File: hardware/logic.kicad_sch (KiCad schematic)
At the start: 23 parts, among them IC1 UCC2946DG4, IC2 SN74LVC1G74DCTR, IC3 SN74LVC1G74DCTR, Q1 BSS123, U1 74157, U2 4011, U3 4081, U4 4071

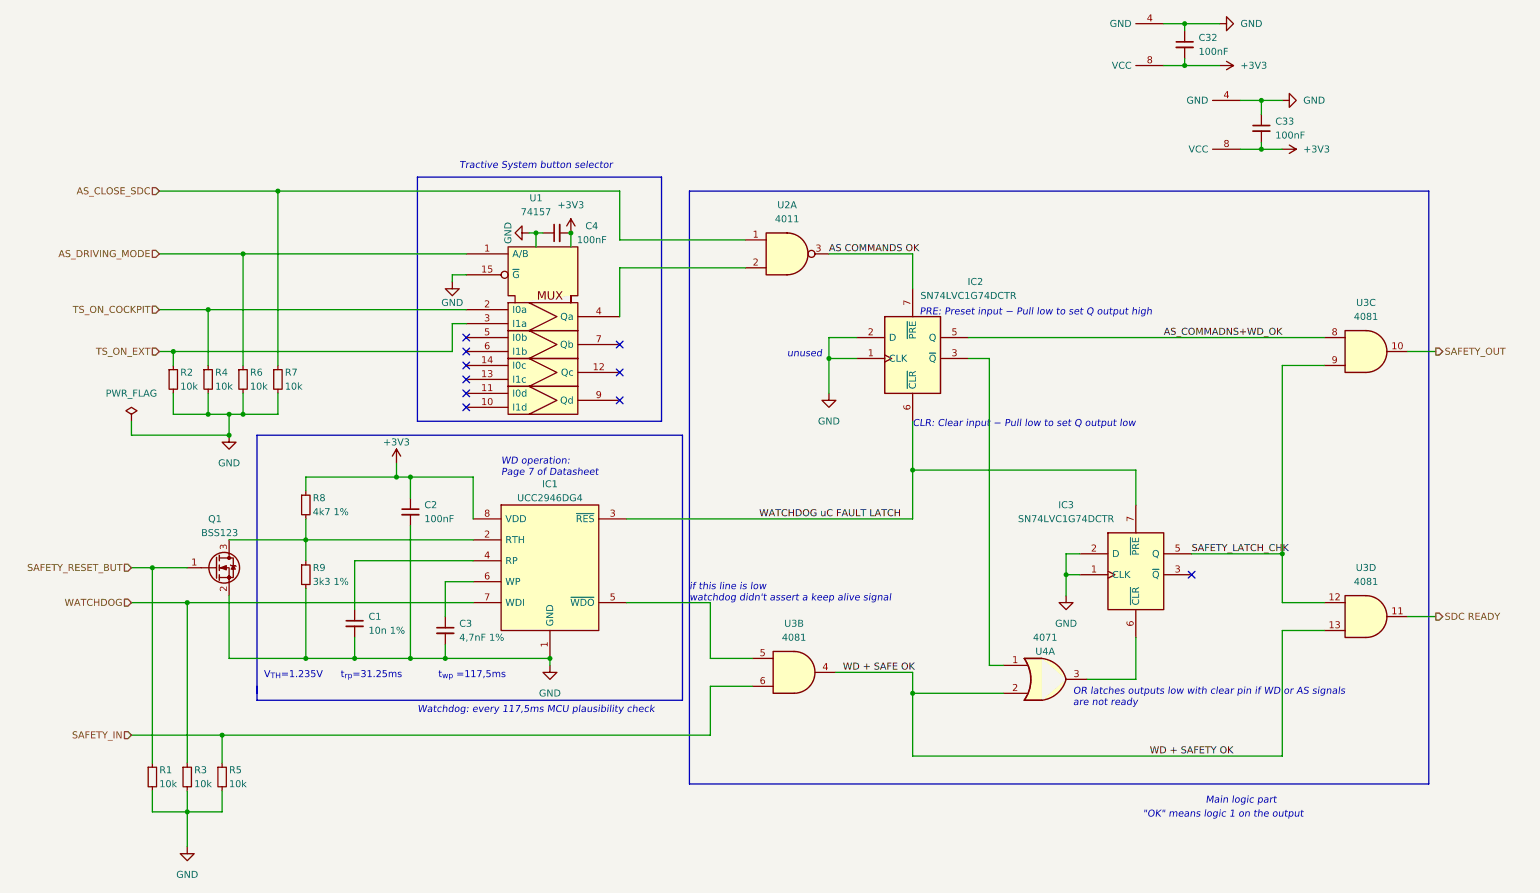
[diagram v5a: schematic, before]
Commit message: 0xERC State
Schematic needs only simulation and veryfying component choice for now
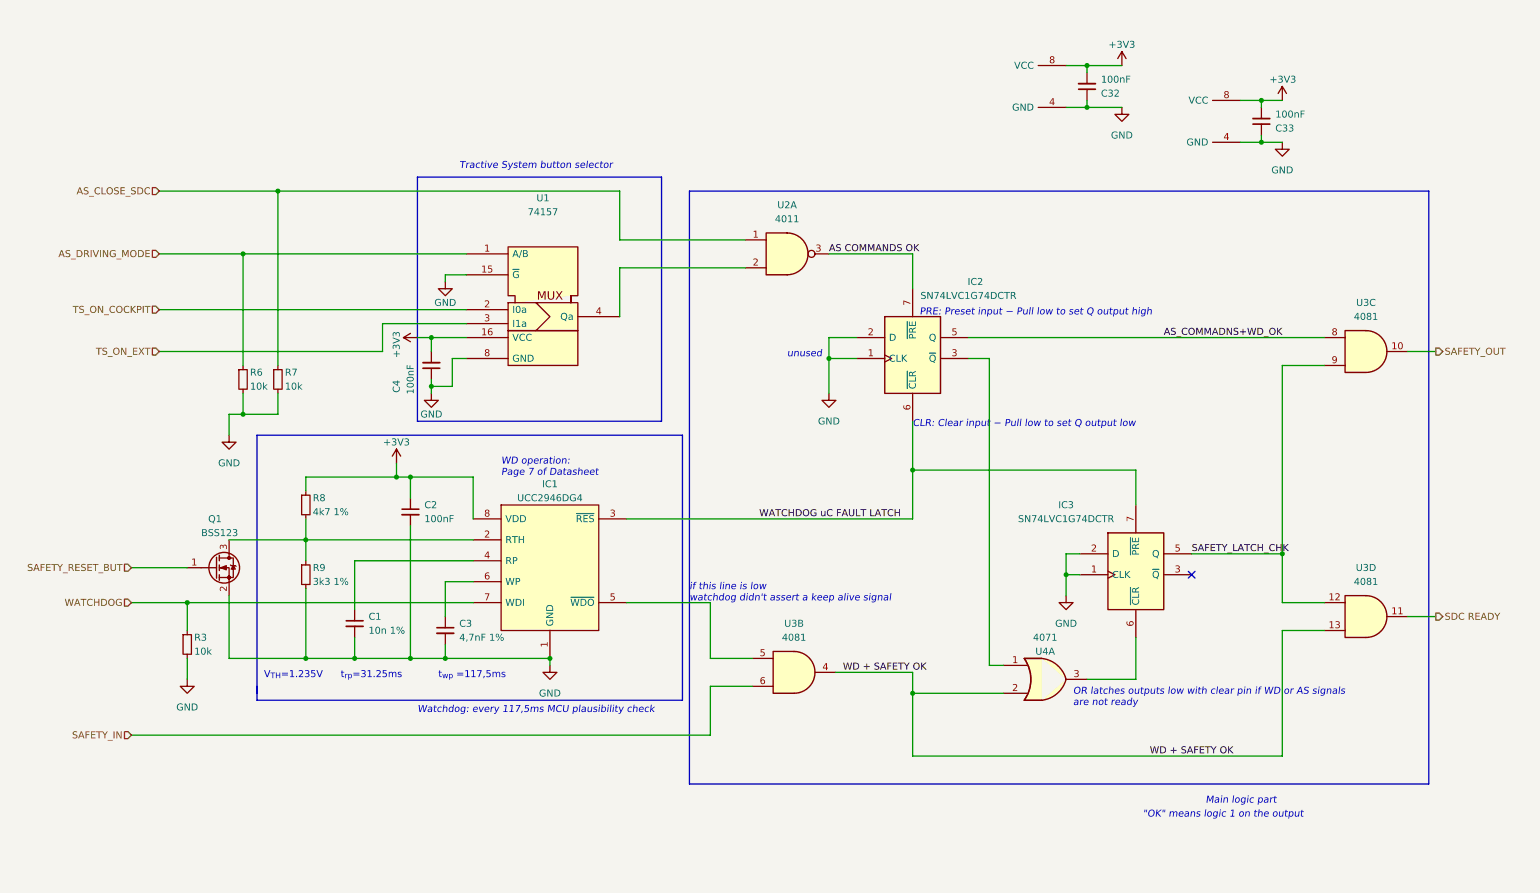
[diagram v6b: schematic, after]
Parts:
- removed R1, R2, R4, R5: 10k, Resistor_SMD:R_0603_1608Metric, symbol Device:R_Small
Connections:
- net WD + SAFE OK renamed WD + SAFETY OK
- no-connect marks 10 -> 1
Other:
- moved on the sheet: C32, C33, C4, IC2, R3

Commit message: working simulations, assigned footprints
"nightly" relase
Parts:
- U1: footprint Resistor_SMD:R_0603_1608Metric -> Package_SO:VSSOP-8_2.3x2mm_P0.5mm
- U2, U3, U4: footprint (none) -> Package_SO:TSSOP-14_4.4x5mm_P0.65mm
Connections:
- net WATCHDOG uC FAULT LATCH renamed RESET BUTTON LATCH
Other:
- note added: "pull RTH low to reset"
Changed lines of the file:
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@@
+    (stroke (width 0) (type default) (color 0 0 0 0))
+  )
+  (wire (pts (xy 187.96 81.28) (xy 187.96 100.33))
     (stroke (width 0) (type default) (color 0 0 0 0))
   )
@@
     (stroke (width 0) (type default) (color 0 0 0 0))
   )
+  (wire (pts (xy 187.96 104.14) (xy 187.96 137.16))
+    (stroke (width 0) (type default) (color 0 0 0 0))
+  )
   (wire (pts (xy 83.82 77.47) (xy 86.36 77.47))
     (stroke (width 0) (type default) (color 0 0 0 0))
@@
     (stroke (width 0) (type default) (color 0 0 0 0))
   )
+  (wire (pts (xy 187.96 100.33) (xy 189.23 100.33))
+    (stroke (width 0) (type default) (color 0 0 0 0))
+  )
   (wire (pts (xy 241.3 130.81) (xy 248.92 130.81))
     (stroke (width 0) (type default) (color 0 0 0 0))
@@
     (stroke (width 0) (type default) (color 0 0 0 0))
   )
-  (wire (pts (xy 187.96 81.28) (xy 187.96 137.16))
-    (stroke (width 0) (type default) (color 0 0 0 0))
-  )
   (wire (pts (xy 41.91 135.89) (xy 41.91 139.7))
     (stroke (width 0) (type default) (color 0 0 0 0))
@@
     (stroke (width 0) (type default) (color 0 0 0 0))
   )
+  (wire (pts (xy 189.23 100.33) (xy 189.23 104.14))
+    (stroke (width 0) (type default) (color 0 0 0 0))
+  )
   (wire (pts (xy 158.75 62.23) (xy 173.99 62.23))
     (stroke (width 0) (type default) (color 0 0 0 0))
@@
   )
   (wire (pts (xy 241.3 125.73) (xy 248.92 125.73))
+    (stroke (width 0) (type default) (color 0 0 0 0))
+  )
+  (wire (pts (xy 189.23 104.14) (xy 187.96 104.14))
     (stroke (width 0) (type default) (color 0 0 0 0))
   )
@@
     (effects (font (size 1.27 1.27) italic) (justify left bottom))
   )
+  (text "pull RTH low to reset\n" (at 22.86 116.84 0)
+    (effects (font (size 1.27 1.27)) (justify left bottom))
+  )
   (text "PRE: Preset input − Pull low to set Q output high" (at 175.26 73.66 0)
     (effects (font (size 1.27 1.27) italic) (justify left bottom))
@@
     (effects (font (size 1.27 1.27)) (justify left bottom))
   )
-  (label "WATCHDOG uC FAULT LATCH" (at 146.05 110.49 0)
+  (label "RESET BUTTON LATCH" (at 146.05 110.49 0)
     (effects (font (size 1.27 1.27)) (justify left bottom))
   )
@@
     (property "Reference" "U4" (id 0) (at 198.12 134.62 0))
     (property "Value" "4071" (id 1) (at 198.12 132.08 0))
-    (property "Footprint" "" (id 2) (at 198.12 139.7 0)
+    (property "Footprint" "Package_SO:TSSOP-14_4.4x5mm_P0.65mm" (id 2) (at 198.12 139.7 0)
       (effects (font (size 1.27 1.27)) hide)
     )
@@
     (property "Reference" "U3" (id 0) (at 256.54 119.38 0))
     (property "Value" "4081" (id 1) (at 256.54 121.92 0))
-    (property "Footprint" "" (id 2) (at 256.54 128.27 0)
+    (property "Footprint" "Package_SO:TSSOP-14_4.4x5mm_P0.65mm" (id 2) (at 256.54 128.27 0)
       (effects (font (size 1.27 1.27)) hide)
     )
@@
     (property "Reference" "U3" (id 0) (at 256.54 71.12 0))
     (property "Value" "4081" (id 1) (at 256.54 73.66 0))
-    (property "Footprint" "" (id 2) (at 256.54 80.01 0)
+    (property "Footprint" "Package_SO:TSSOP-14_4.4x5mm_P0.65mm" (id 2) (at 256.54 80.01 0)
       (effects (font (size 1.27 1.27)) hide)
     )
@@
     (property "Reference" "U2" (id 0) (at 151.13 53.34 0))
     (property "Value" "4011" (id 1) (at 151.13 55.88 0))
-    (property "Footprint" "" (id 2) (at 151.13 62.23 0)
+    (property "Footprint" "Package_SO:TSSOP-14_4.4x5mm_P0.65mm" (id 2) (at 151.13 62.23 0)
       (effects (font (size 1.27 1.27)) hide)
     )
@@
     (property "Reference" "U1" (id 0) (at 106.68 52.07 0))
     (property "Value" "74157" (id 1) (at 106.68 54.61 0))
-    (property "Footprint" "Resistor_SMD:R_0603_1608Metric" (id 2) (at 127 58.42 0)
+    (property "Footprint" "Package_SO:VSSOP-8_2.3x2mm_P0.5mm" (id 2) (at 127 58.42 0)
       (effects (font (size 1.27 1.27)) hide)
     )
@@
     (property "Reference" "U3" (id 0) (at 152.4 129.54 0))
     (property "Value" "4081" (id 1) (at 152.4 132.08 0))
-    (property "Footprint" "" (id 2) (at 152.4 138.43 0)
-      (effects (font (size 1.27 1.27)) hide)
-    )
+    (property "Footprint" "Package_SO:TSSOP-14_4.4x5mm_P0.65mm" (id 2) (at 152.4 138.43 0)
+      (effects (font (size 1.27 1.27)) hide)
+    )

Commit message: minor changes
pre spotkanie comiit ;DD
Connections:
- net +3V3: now also U1.8 (VCC); no longer U1.16 (VCC)
- net AS_DRIVING_MODE: now also U1.6 (A/B); no longer U1.1 (A/B)
- net GND: now also U1.4 (GND), U1.7 (~{G}); no longer U1.15 (~{G}), U1.8 (GND)
- net TS_ON_COCKPIT: now also U1.1 (I0a); no longer U1.2 (I0a)
- net TS_ON_EXT: now also U1.2 (I1a); no longer U1.3 (I1a)
- net at U2.2: now also U1.5 (Qa); no longer U1.4 (Qa)
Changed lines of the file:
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@@
       (effects (font (size 1.27 1.27)) hide)
     )
-    (pin "16")
     (pin "8")
-    (pin "1")
-    (pin "10")
-    (pin "11")
-    (pin "12")
-    (pin "13")
-    (pin "14")
-    (pin "15")
-    (pin "2")
-    (pin "3")
     (pin "4")
-    (pin "5")
     (pin "6")
     (pin "7")
-    (pin "9")
+    (pin "1")
+    (pin "2")
+    (pin "5")
+    (pin "3")
   )
   (symbol (lib_id "power:GND") (at 107.95 137.16 0) (unit 1)
